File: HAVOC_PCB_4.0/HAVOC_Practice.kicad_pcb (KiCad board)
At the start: 2 copper layers, 90 x 100 mm, 49 parts, among them J1 132134, J10 BATT/switch, J3 NG, J7 solenoid, J8 Micro_SD_Card, J9 BNO, Q1 NMOS, Q2 NMOS, Q3 NMOS, Q4 NMOS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

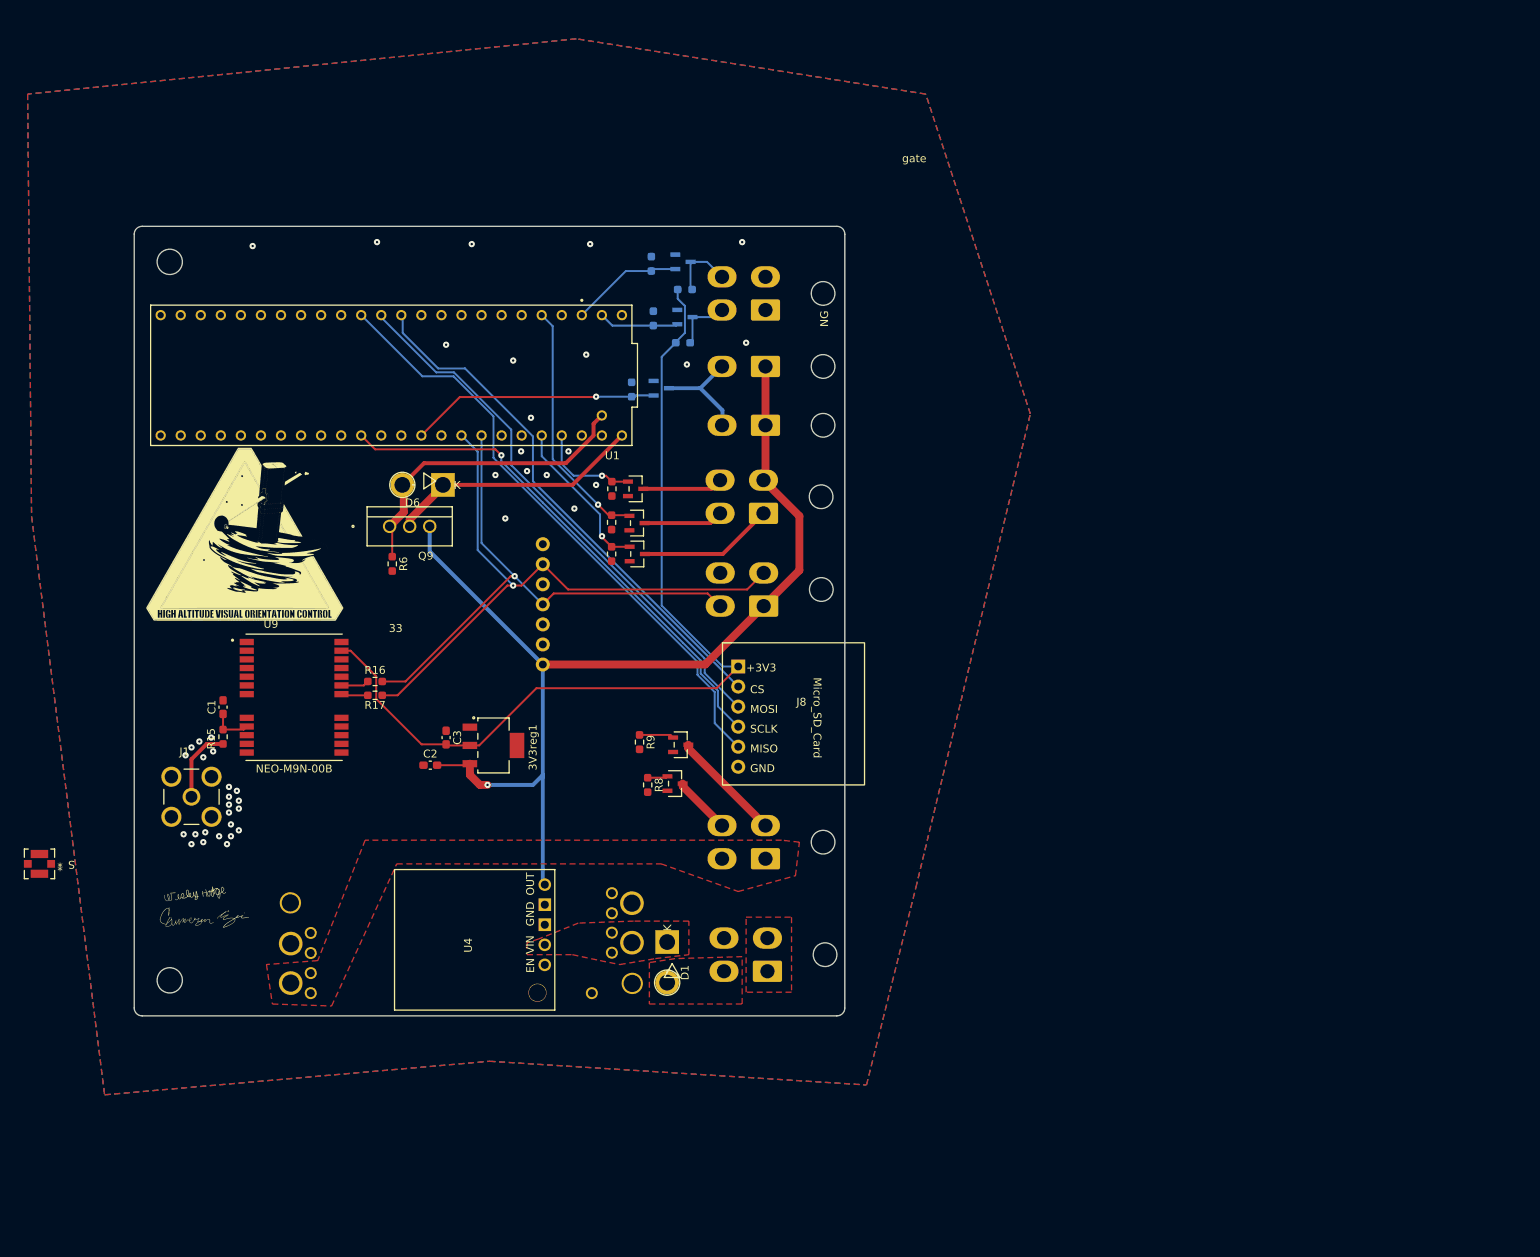
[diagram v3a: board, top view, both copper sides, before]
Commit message: added backup battery and fixed missing PWM lines
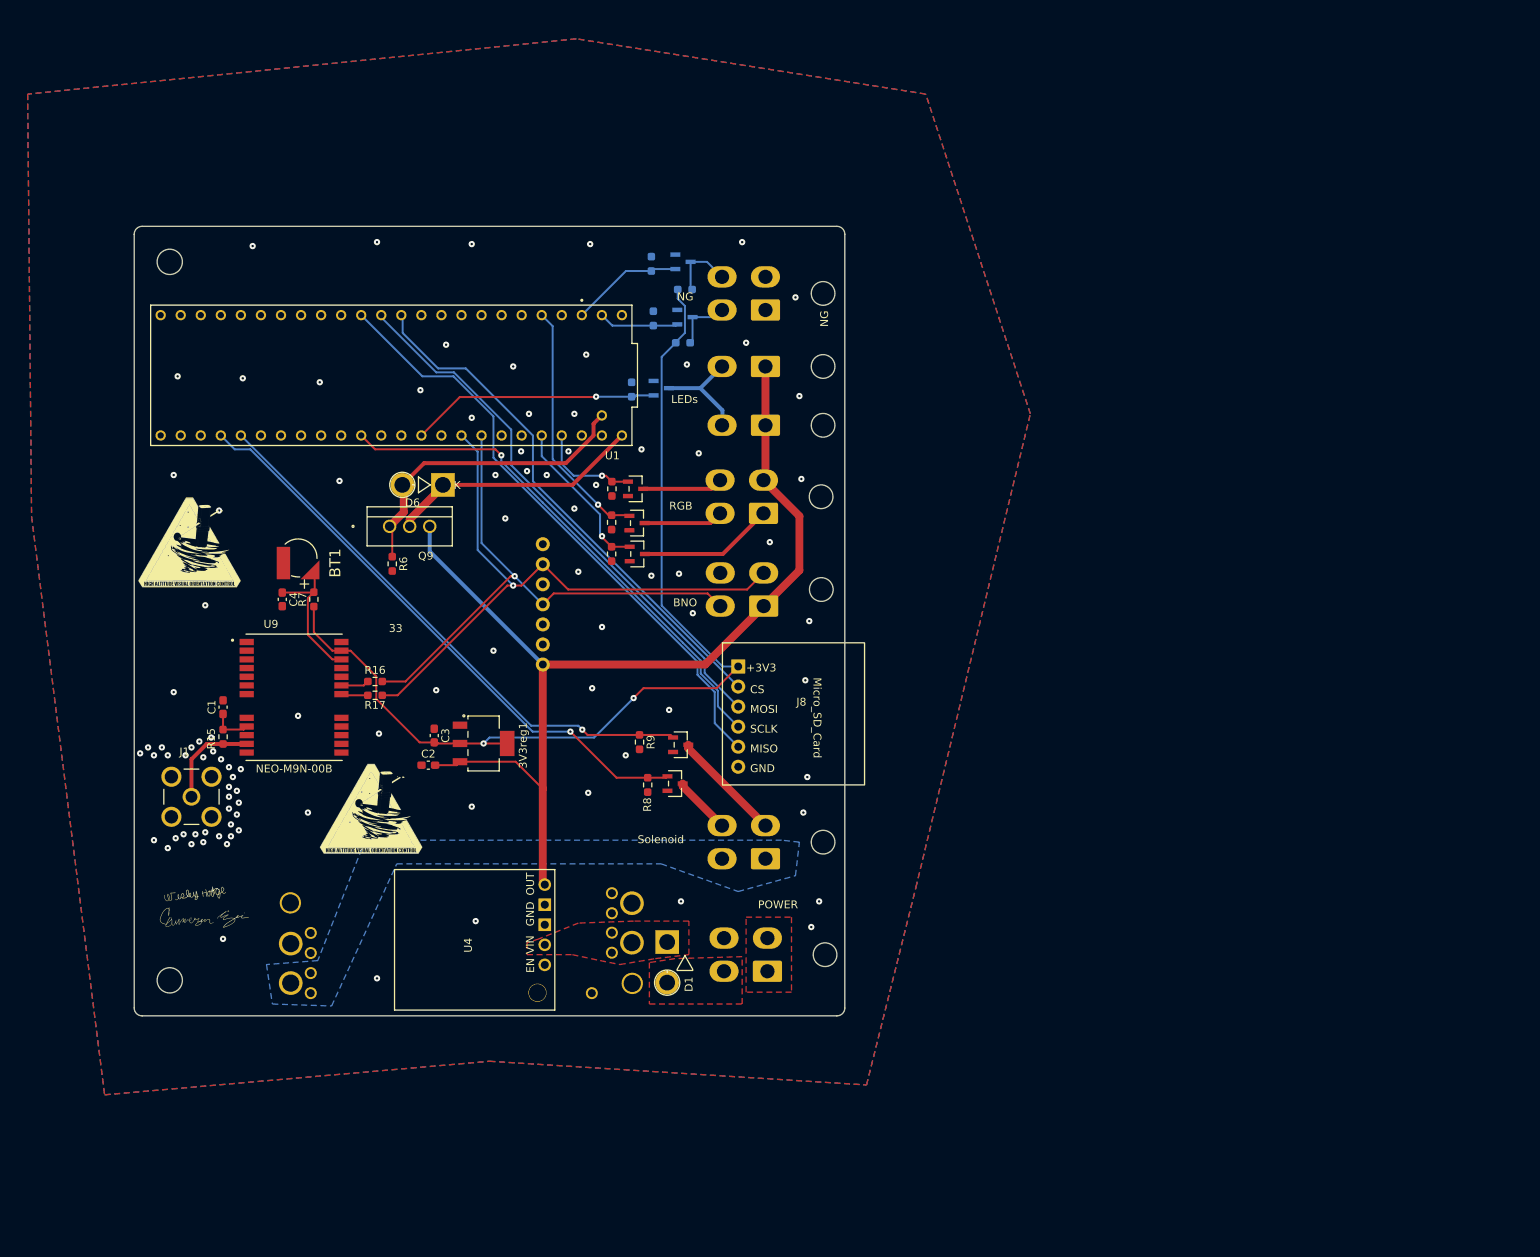
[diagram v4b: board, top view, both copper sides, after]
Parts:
- removed AE1: Antenna_Shield, SHC:antennaufl
- added BT1: Battery_Cell, SHC:GPS_BATT, F.Cu at (54.8, 89.0)
- added C4: 1.0uF, Capacitor_SMD:C_0603_1608Metric_Pad1.08x0.95mm_HandSolder, F.Cu at (52.8, 94.2)
- added G***: LOGO, LOGO, F.Cu at (64.0, 121.0)
- added G***: LOGO, LOGO, F.Cu at (41.0, 87.2)
- added R7: 1K, Resistor_SMD:R_0603_1608Metric_Pad0.98x0.95mm_HandSolder, F.Cu at (56.8, 94.2)
- G***: moved to B.Cu
- moved G*** 6.89 mm to (49.0, 93.2), turned to 180 degrees
- moved C3 1.52 mm to (72.0, 111.5)
- moved 3V3reg1 1.27 mm to (78.2, 112.5)
- moved C2 0.25 mm to (71.2, 115.2)
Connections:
- U1 pad 14: /PWM1 -> unconnected-(U1-A0-Pad14)
- U1 pad 15: /PWM2 -> unconnected-(U1-A1-Pad15)
- U1 pad 36: unconnected-(U1-CS2-Pad36) -> /PWM2
- U1 pad 37: unconnected-(U1-CS3-Pad37) -> /PWM1
- U9 pad 22: unconnected-(U9-V_BCKP-Pad22) -> /GPS_BATT
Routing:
- net /PWM2: track 2.57 -> 74.7 mm, vias 0 -> 1
- net /PWM1: track 4.39 -> 70.8 mm, vias 0 -> 1
- net /GPS_BATT: track 0.00 -> 17.6 mm
- net +3V3: track 115.6 -> 126.0 mm, vias 0 -> 2
- net Net-(U9-RF_IN): track 9.55 -> 12.6 mm
- net +5V: track 132.6 -> 132.3 mm, vias 1 -> 0
- net GND: track 0.00 -> 0.09 mm, vias 42 -> 95
- added copper zone on B.Cu, net +12V
- removed copper zone on F.Cu, net +12V
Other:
- board text added: "LEDs"
- board text added: "POWER"
- board text added: "RGB"
- board text added: "Solenoid"
- board text removed: "gate"

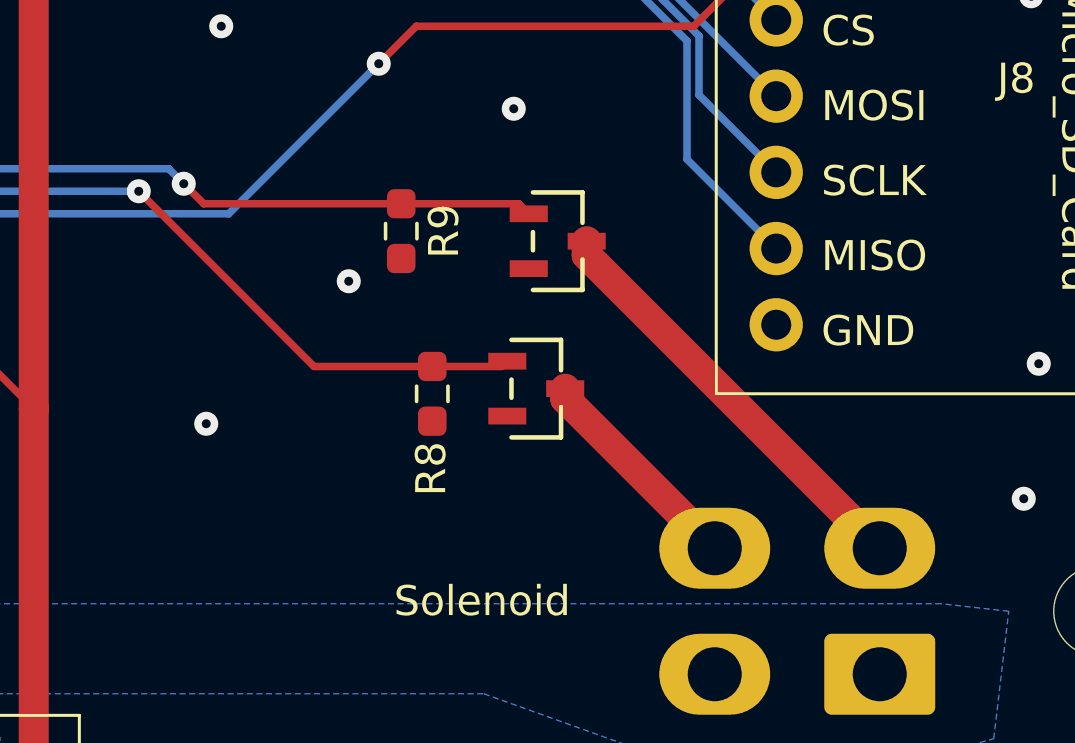
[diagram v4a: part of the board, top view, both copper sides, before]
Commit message: made mosfets for solenoids aligned so cam won't be displeased
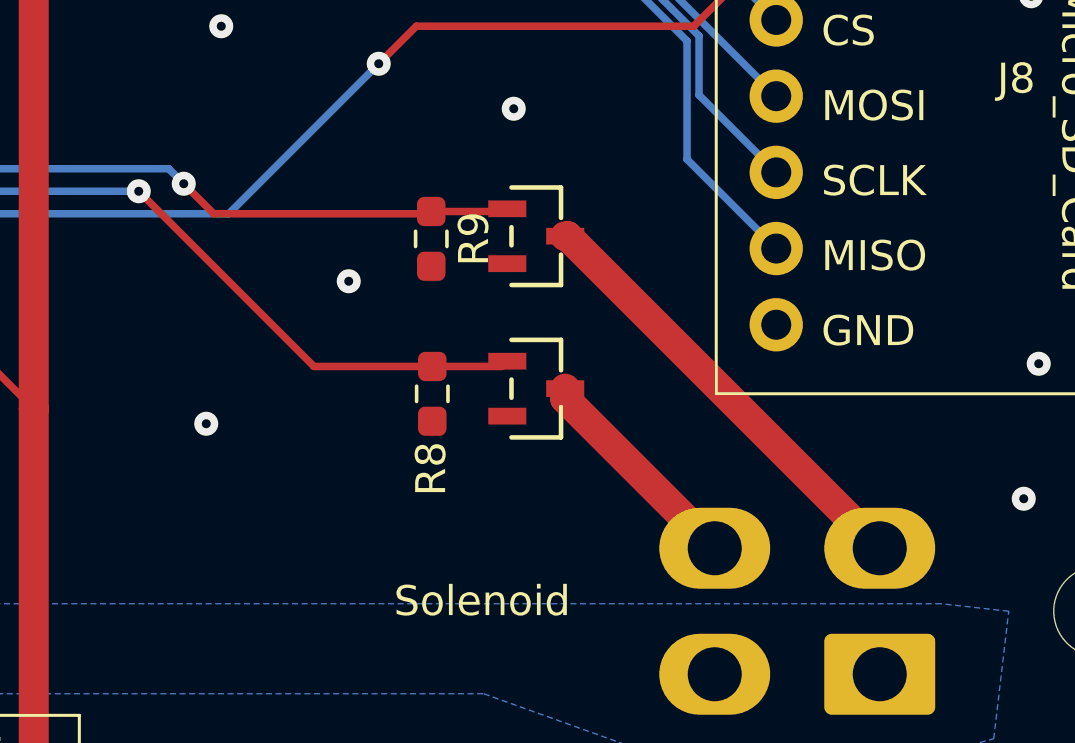
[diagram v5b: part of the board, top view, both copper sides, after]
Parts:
- moved R9 1.03 mm to (99.0, 112.6)
- moved Q1 0.73 mm to (102.5, 112.5)
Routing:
- net /PWM1: track 70.8 -> 70.3 mm
- net Net-(J7-Pin_2): track 14.3 -> 14.8 mm
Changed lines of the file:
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@@
 	(footprint "SHC:SOT23_DMG3406_DIO"
 		(layer "F.Cu")
-		(at 103.2152 112.664999 -90)
+		(at 102.5 112.5 -90)
 		(tags "DMG3406L-13 ")
 		(property "Reference" "Q1"
@@
 	(footprint "Resistor_SMD:R_0603_1608Metric_Pad0.98x0.95mm_HandSolder"
 		(layer "F.Cu")
-		(at 98 112.329998 -90)
+		(at 99 112.5875 -90)
 		(descr "Resistor SMD 0603 (1608 Metric), square (rectangular) end terminal, IPC_7351 nominal with elongated pad for handsoldering. (Body size source: IPC-SM-782 page 72, https://www.pcb-3d.com/wordpress/wp-content/uploads/ipc-sm-782a_amendment_1_and_2.pdf), generated with kicad-footprint-generator")
 		(tags "resistor handsolder")
@@
 	)
 	(segment
-		(start 90.75 110.75)
-		(end 91.417498 111.417498)
+		(start 99.3375 111.5875)
+		(end 99.339999 111.585001)
+		(width 0.25)
+		(layer "F.Cu")
+		(net 19)
+	)
+	(segment
+		(start 99 111.5875)
+		(end 99.3375 111.5875)
+		(width 0.25)
+		(layer "F.Cu")
+		(net 19)
+	)
+	(segment
+		(start 98.925 111.75)
+		(end 99 111.675)
 		(width 0.25)
 		(layer "F.Cu")
@@
 	)
 	(segment
-		(start 91.417498 111.417498)
-		(end 98 111.417498)
+		(start 91.75 111.75)
+		(end 98.925 111.75)
 		(width 0.25)
 		(layer "F.Cu")
@@
 	)
 	(segment
-		(start 101.917498 111.417498)
-		(end 102.25 111.75)
+		(start 99 111.675)
+		(end 101.444801 111.675)
 		(width 0.25)
 		(layer "F.Cu")
@@
 	)
 	(segment
-		(start 97.832502 111.25)
-		(end 98 111.417498)
+		(start 101.444801 111.675)
+		(end 101.5348 111.585001)
 		(width 0.25)
 		(layer "F.Cu")
@@
 	)
 	(segment
-		(start 98 111.417498)
-		(end 101.917498 111.417498)
+		(start 90.75 110.75)
+		(end 91.75 111.75)
 		(width 0.25)
 		(layer "F.Cu")
@@
 	)
 	(segment
-		(start 104.1804 112.664999)
-		(end 104.1804 113.1304)
+		(start 103.55 112.5)
+		(end 113.95 122.9)
 		(width 1)
 		(layer "F.Cu")
@@
 	)
 	(segment
-		(start 104.1804 113.1304)
-		(end 113.95 122.9)
+		(start 103.4652 112.5)
+		(end 103.55 112.5)
 		(width 1)
 		(layer "F.Cu")
